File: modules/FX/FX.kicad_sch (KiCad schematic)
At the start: 32 parts, among them J9 Conn_01x13, U2 TL072, U3 TL074

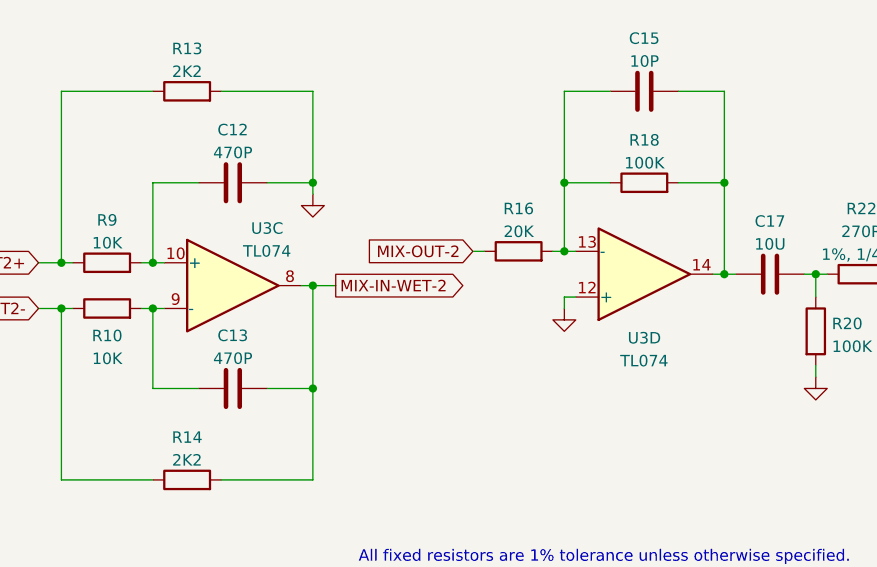
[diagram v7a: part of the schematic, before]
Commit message: FX module - update TODO
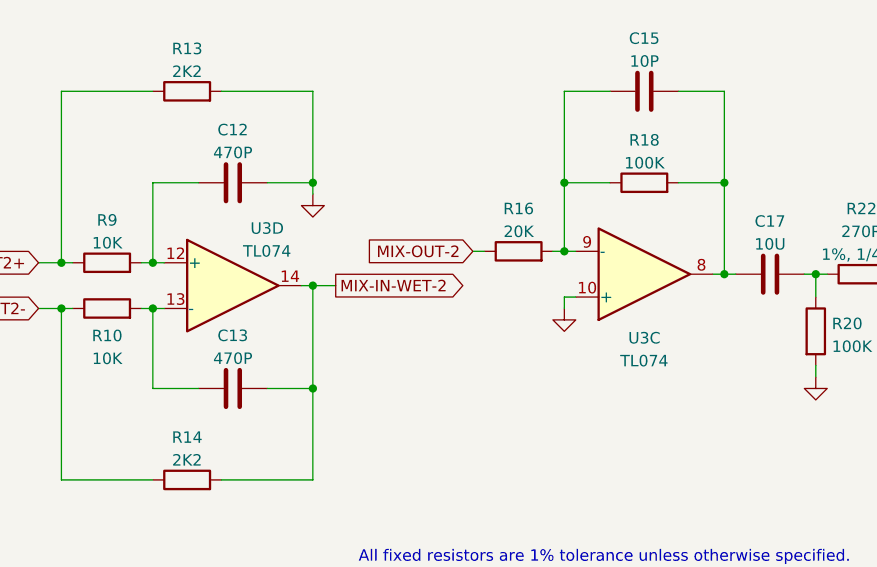
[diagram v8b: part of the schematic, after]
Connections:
- net GND: now also U3.10 (+); no longer U3.12 (+)
- net MIX-IN-WET-2: now also U3.14; no longer U3.8
- net at C15.1, R16.2, R18.1: now also U3.9 (-); no longer U3.13 (-)
- net at C15.2, C17.1, R18.2: now also U3.8; no longer U3.14
- net at C12.1, R9.2: now also U3.12 (+); no longer U3.10 (+)
- net at C13.1, R10.2: now also U3.13 (-); no longer U3.9 (-)
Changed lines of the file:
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@@
     (pin "2")
   )
-  (symbol (lib_id "-lmp-opamp:TL074") (at 163.83 123.19 0) (unit 3)
+  (symbol (lib_id "-lmp-opamp:TL074") (at 163.83 123.19 0) (unit 4)
     (in_bom yes) (on_board yes)
     (property "Reference" "U3" (id 0) (at 167.64 116.84 0))
@@
     (pin "2")
   )
-  (symbol (lib_id "-lmp-opamp:TL074") (at 209.55 121.92 0) (mirror x) (unit 4)
+  (symbol (lib_id "-lmp-opamp:TL074") (at 209.55 121.92 0) (mirror x) (unit 3)
     (in_bom yes) (on_board yes) (fields_autoplaced)
     (property "Reference" "U3" (id 0) (at 209.55 129.0304 0))
@@
       (reference "U3") (unit 2) (value "TL074") (footprint "Package_DIP:DIP-14_W7.62mm")
     )
+    (path "/e2d39f50-e0d4-4e9b-b538-d9a5019f496f"
+      (reference "U3") (unit 3) (value "TL074") (footprint "Package_DIP:DIP-14_W7.62mm")
+    )
     (path "/74c48025-a80d-487d-8ec3-c569d56ebd75"
-      (reference "U3") (unit 3) (value "TL074") (footprint "Package_DIP:DIP-14_W7.62mm")
-    )
-    (path "/e2d39f50-e0d4-4e9b-b538-d9a5019f496f"
       (reference "U3") (unit 4) (value "TL074") (footprint "Package_DIP:DIP-14_W7.62mm")
     )
